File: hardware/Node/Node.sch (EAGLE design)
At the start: 67 parts, among them J1 AVR_SPI_PRG_6NS, J2 M04X2, Q1 PMR280UN, Q2 PMR280UN, Q3 PMR280UN, SW1 KSS, SW2 KSS, U1 ATMEGA32U4QFN, U2 BLUETOOTH-RN41", U3 LSM303DLM, U4 L3GD20, U5 8.0MHz, U6 MCP73871, U7 V_REG_LDOSMD, U9 RCLAMP0502A, X1 USBSMD

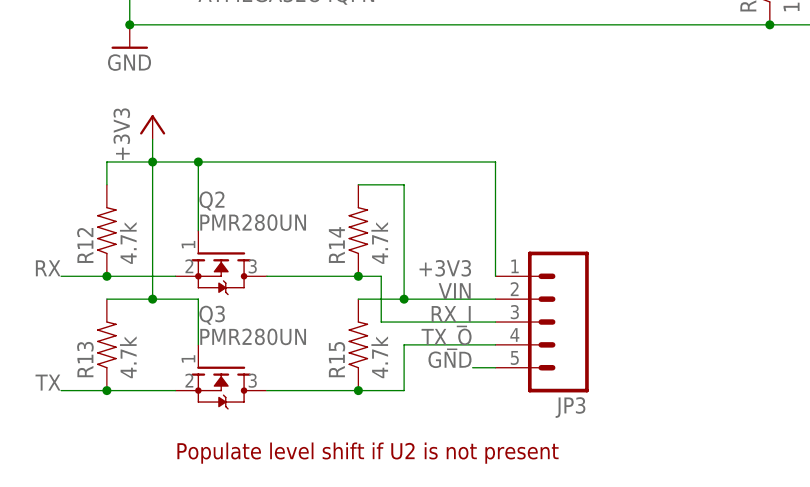
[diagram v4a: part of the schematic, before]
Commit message: put vbus on the header
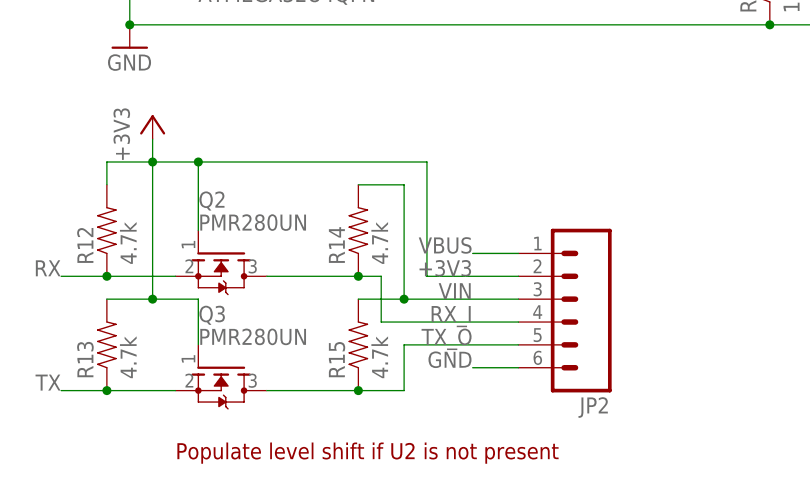
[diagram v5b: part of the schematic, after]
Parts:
- removed JP3: (no value), SparkFun:M05PTH
- added JP2: (no value), SparkFun:M06SIP
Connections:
- net +3V3: now also JP2.2; no longer JP3.1
- net GND: now also JP2.6; no longer JP3.5
- net RX_I: now also JP2.4; no longer JP3.3
- net TX_O: now also JP2.5; no longer JP3.4
- net VBUS: now also JP2.1
- net VIN: now also JP2.3; no longer JP3.2
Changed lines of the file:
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@@
 <grid distance="0.1" unitdist="inch" unit="inch" style="lines" multiple="1" display="no" altdistance="0.01" altunitdist="inch" altunit="inch"/>
 <layers>
-<layer number="1" name="Top" color="4" fill="1" visible="yes" active="no"/>
-<layer number="16" name="Bottom" color="1" fill="1" visible="yes" active="no"/>
-<layer number="17" name="Pads" color="2" fill="1" visible="yes" active="no"/>
-<layer number="18" name="Vias" color="2" fill="1" visible="yes" active="no"/>
-<layer number="19" name="Unrouted" color="6" fill="1" visible="yes" active="no"/>
-<layer number="20" name="Dimension" color="15" fill="1" visible="yes" active="no"/>
-<layer number="21" name="tPlace" color="7" fill="1" visible="yes" active="no"/>
-<layer number="22" name="bPlace" color="7" fill="1" visible="yes" active="no"/>
-<layer number="23" name="tOrigins" color="15" fill="1" visible="yes" active="no"/>
-<layer number="24" name="bOrigins" color="15" fill="1" visible="yes" active="no"/>
-<layer number="25" name="tNames" color="7" fill="1" visible="yes" active="no"/>
-<layer number="26" name="bNames" color="7" fill="1" visible="yes" active="no"/>
-<layer number="27" name="tValues" color="7" fill="1" visible="yes" active="no"/>
-<layer number="28" name="bValues" color="7" fill="1" visible="yes" active="no"/>
+<layer number="1" name="Top" color="4" fill="1" visible="no" active="no"/>
+<layer number="16" name="Bottom" color="1" fill="1" visible="no" active="no"/>
+<layer number="17" name="Pads" color="2" fill="1" visible="no" active="no"/>
+<layer number="18" name="Vias" color="2" fill="1" visible="no" active="no"/>
+<layer number="19" name="Unrouted" color="6" fill="1" visible="no" active="no"/>
+<layer number="20" name="Dimension" color="15" fill="1" visible="no" active="no"/>
+<layer number="21" name="tPlace" color="7" fill="1" visible="no" active="no"/>
+<layer number="22" name="bPlace" color="7" fill="1" visible="no" active="no"/>
+<layer number="23" name="tOrigins" color="15" fill="1" visible="no" active="no"/>
+<layer number="24" name="bOrigins" color="15" fill="1" visible="no" active="no"/>
+<layer number="25" name="tNames" color="7" fill="1" visible="no" active="no"/>
+<layer number="26" name="bNames" color="7" fill="1" visible="no" active="no"/>
+<layer number="27" name="tValues" color="7" fill="1" visible="no" active="no"/>
+<layer number="28" name="bValues" color="7" fill="1" visible="no" active="no"/>
 <layer number="29" name="tStop" color="7" fill="3" visible="no" active="no"/>
 <layer number="30" name="bStop" color="7" fill="6" visible="no" active="no"/>
@@
 <layer number="35" name="tGlue" color="7" fill="4" visible="no" active="no"/>
 <layer number="36" name="bGlue" color="7" fill="5" visible="no" active="no"/>
-<layer number="37" name="tTest" color="7" fill="1" visible="yes" active="no"/>
-<layer number="38" name="bTest" color="7" fill="1" visible="yes" active="no"/>
+<layer number="37" name="tTest" color="7" fill="1" visible="no" active="no"/>
+<layer number="38" name="bTest" color="7" fill="1" visible="no" active="no"/>
 <layer number="39" name="tKeepout" color="4" fill="11" visible="no" active="no"/>
 <layer number="40" name="bKeepout" color="1" fill="11" visible="no" active="no"/>
@@
 <layer number="44" name="Drills" color="7" fill="1" visible="no" active="no"/>
 <layer number="45" name="Holes" color="7" fill="1" visible="no" active="no"/>
-<layer number="46" name="Milling" color="3" fill="1" visible="yes" active="no"/>
-<layer number="47" name="Measures" color="7" fill="1" visible="yes" active="no"/>
-<layer number="48" name="Document" color="7" fill="1" visible="yes" active="no"/>
-<layer number="49" name="Reference" color="7" fill="1" visible="yes" active="no"/>
-<layer number="50" name="dxf" color="7" fill="1" visible="yes" active="no"/>
-<layer number="51" name="tDocu" color="7" fill="1" visible="yes" active="no"/>
-<layer number="52" name="bDocu" color="7" fill="1" visible="yes" active="no"/>
-<layer number="53" name="tGND_GNDA" color="7" fill="9" visible="yes" active="no"/>
-<layer number="54" name="bGND_GNDA" color="1" fill="9" visible="yes" active="no"/>
-<layer number="56" name="wert" color="7" fill="1" visible="yes" active="no"/>
+<layer number="46" name="Milling" color="3" fill="1" visible="no" active="no"/>
+<layer number="47" name="Measures" color="7" fill="1" visible="no" active="no"/>
+<layer number="48" name="Document" color="7" fill="1" visible="no" active="no"/>
+<layer number="49" name="Reference" color="7" fill="1" visible="no" active="no"/>
+<layer number="50" name="dxf" color="7" fill="1" visible="no" active="no"/>
+<layer number="51" name="tDocu" color="7" fill="1" visible="no" active="no"/>
+<layer number="52" name="bDocu" color="7" fill="1" visible="no" active="no"/>
+<layer number="53" name="tGND_GNDA" color="7" fill="9" visible="no" active="no"/>
+<layer number="54" name="bGND_GNDA" color="1" fill="9" visible="no" active="no"/>
+<layer number="56" name="wert" color="7" fill="1" visible="no" active="no"/>
 <layer number="91" name="Nets" color="2" fill="1" visible="yes" active="yes"/>
 <layer number="92" name="Busses" color="1" fill="1" visible="yes" active="yes"/>
@@
 <part name="LED1" library="SparkFun" deviceset="LED" device="0603"/>
 <part name="R20" library="SparkFun" deviceset="RESISTOR" device="0402-RES" value="1k"/>
-<part name="JP3" library="SparkFun" deviceset="M05" device="PTH"/>
 <part name="R10" library="SparkFun" deviceset="RESISTOR" device="0402-RES" value="100k"/>
 <part name="R11" library="SparkFun" deviceset="RESISTOR" device="0402-RES" value="100k"/>
 <part name="J2" library="SparkFun" deviceset="M04X2" device=""/>
 <part name="+3V9" library="supply1" deviceset="+3V3" device=""/>
+<part name="JP2" library="SparkFun" deviceset="M06" device="SIP"/>
 </parts>
 <sheets>
@@
 <instance part="LED1" gate="G$1" x="50.8" y="203.2"/>
 <instance part="R20" gate="G$1" x="50.8" y="193.04" rot="R90"/>
-<instance part="JP3" gate="G$1" x="147.32" y="20.32" rot="R180"/>
 <instance part="R10" gate="G$1" x="157.48" y="187.96" rot="R90"/>
 <instance part="R11" gate="G$1" x="157.48" y="172.72" rot="R90"/>
 <instance part="J2" gate="G$1" x="160.02" y="132.08"/>
 <instance part="+3V9" gate="G$1" x="149.86" y="139.7"/>
+<instance part="JP2" gate="G$1" x="147.32" y="22.86" rot="R180"/>
 </instances>
 <busses>
@@
 </segment>
 <segment>
-<wire x1="139.7" y1="15.24" x2="137.16" y2="15.24" width="0.1524" layer="91"/>
+<wire x1="142.24" y1="15.24" x2="137.16" y2="15.24" width="0.1524" layer="91"/>
 <label x="137.16" y="15.24" size="1.778" layer="95" rot="MR0"/>
-<pinref part="JP3" gate="G$1" pin="5"/>
+<pinref part="JP2" gate="G$1" pin="6"/>
 </segment>
 <segment>
@@
 <wire x1="96.52" y1="35.56" x2="96.52" y2="38.1" width="0.1524" layer="91"/>
 <wire x1="96.52" y1="38.1" x2="101.6" y2="38.1" width="0.1524" layer="91"/>
-<wire x1="106.68" y1="38.1" x2="139.7" y2="38.1" width="0.1524" layer="91"/>
+<wire x1="106.68" y1="38.1" x2="132.08" y2="38.1" width="0.1524" layer="91"/>
+<wire x1="132.08" y1="38.1" x2="132.08" y2="25.4" width="0.1524" layer="91"/>
 <junction x="106.68" y="38.1"/>
-<pinref part="JP3" gate="G$1" pin="1"/>
-<wire x1="139.7" y1="38.1" x2="139.7" y2="25.4" width="0.1524" layer="91"/>
+<pinref part="JP2" gate="G$1" pin="2"/>
+<wire x1="132.08" y1="25.4" x2="142.24" y2="25.4" width="0.1524" layer="91"/>
 <label x="137.16" y="25.4" size="1.778" layer="95" rot="MR0"/>
 </segment>
@@
 <pinref part="U9" gate="G$1" pin="VCC"/>
 </segment>
+<segment>
+<pinref part="JP2" gate="G$1" pin="1"/>
+<wire x1="142.24" y1="27.94" x2="137.16" y2="27.94" width="0.1524" layer="91"/>
+<label x="137.16" y="27.94" size="1.778" layer="95" rot="MR0"/>
+</segment>
 </net>
 <net name="RX" class="0">
@@
 <pinref part="R14" gate="G$1" pin="1"/>
 <wire x1="124.46" y1="25.4" x2="114.3" y2="25.4" width="0.1524" layer="91"/>
-<wire x1="139.7" y1="20.32" x2="127" y2="20.32" width="0.1524" layer="91"/>
+<wire x1="142.24" y1="20.32" x2="127" y2="20.32" width="0.1524" layer="91"/>
 <wire x1="127" y1="20.32" x2="127" y2="25.4" width="0.1524" layer="91"/>
 <wire x1="127" y1="25.4" x2="124.46" y2="25.4" width="0.1524" layer="91"/>
 <junction x="124.46" y="25.4"/>
 <label x="137.16" y="20.32" size="1.778" layer="95" rot="MR0"/>
-<pinref part="JP3" gate="G$1" pin="3"/>
+<pinref part="JP2" gate="G$1" pin="4"/>
 </segment>
 </net>
@@
 <pinref part="R15" gate="G$1" pin="1"/>
 <wire x1="124.46" y1="12.7" x2="114.3" y2="12.7" width="0.1524" layer="91"/>
-<wire x1="139.7" y1="17.78" x2="129.54" y2="17.78" width="0.1524" layer="91"/>
+<wire x1="142.24" y1="17.78" x2="129.54" y2="17.78" width="0.1524" layer="91"/>
 <wire x1="129.54" y1="17.78" x2="129.54" y2="12.7" width="0.1524" layer="91"/>
 <wire x1="129.54" y1="12.7" x2="124.46" y2="12.7" width="0.1524" layer="91"/>
 <junction x="124.46" y="12.7"/>
 <label x="137.16" y="17.78" size="1.778" layer="95" rot="MR0"/>
-<pinref part="JP3" gate="G$1" pin="4"/>
+<pinref part="JP2" gate="G$1" pin="5"/>
 </segment>
 </net>
@@
 <segment>
 <pinref part="R15" gate="G$1" pin="2"/>
-<wire x1="139.7" y1="22.86" x2="129.54" y2="22.86" width="0.1524" layer="91"/>
+<wire x1="142.24" y1="22.86" x2="129.54" y2="22.86" width="0.1524" layer="91"/>
 <pinref part="R14" gate="G$1" pin="2"/>
 <wire x1="129.54" y1="22.86" x2="124.46" y2="22.86" width="0.1524" layer="91"/>
@@
 <junction x="129.54" y="22.86"/>
 <label x="137.16" y="22.86" size="1.778" layer="95" rot="MR0"/>
-<pinref part="JP3" gate="G$1" pin="2"/>
-</segment>
-</net>
+<pinref part="JP2" gate="G$1" pin="3"/>
+</segment>
+</net>

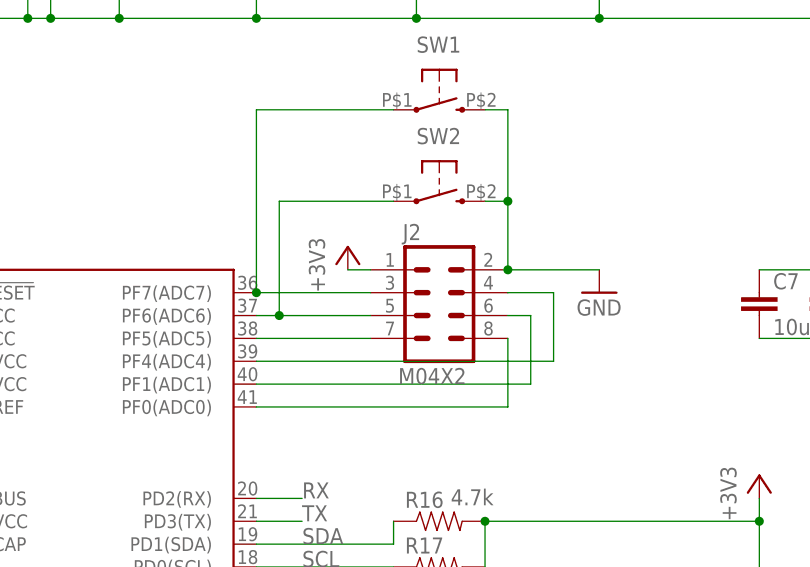
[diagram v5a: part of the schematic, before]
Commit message: route more of the breakouts
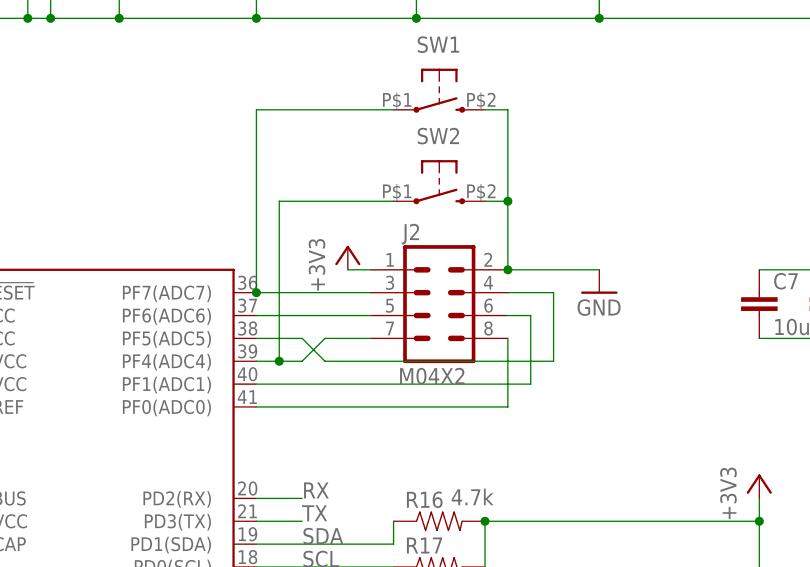
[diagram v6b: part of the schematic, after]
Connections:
- removed net N$31: J2.5, SW2.1, U1.PF6(ADC6)
- removed net N$33: J2.4, U1.PF4(ADC4)
- new net N$15: J2.4, U1.PF5(ADC5)
- new net N$30: J2.7, SW2.1, U1.PF4(ADC4)
- net N$32: now also J2.5, U1.PF6(ADC6); no longer J2.7, U1.PF5(ADC5)
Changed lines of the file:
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@@
-</segment>
-</net>
-<net name="N$31" class="0">
-<segment>
-<pinref part="U1" gate="G$1" pin="PF6(ADC6)"/>
-<wire x1="139.7" y1="132.08" x2="142.24" y2="132.08" width="0.1524" layer="91"/>
-<pinref part="SW2" gate="G$1" pin="1"/>
-<wire x1="142.24" y1="132.08" x2="152.4" y2="132.08" width="0.1524" layer="91"/>
-<wire x1="154.94" y1="144.78" x2="142.24" y2="144.78" width="0.1524" layer="91"/>
-<wire x1="142.24" y1="144.78" x2="142.24" y2="132.08" width="0.1524" layer="91"/>
-<junction x="142.24" y="132.08"/>
-<pinref part="J2" gate="G$1" pin="5"/>
-</segment>
-</net>
-<net name="N$32" class="0">
-<segment>
-<pinref part="U1" gate="G$1" pin="PF5(ADC5)"/>
-<wire x1="139.7" y1="129.54" x2="152.4" y2="129.54" width="0.1524" layer="91"/>
-<pinref part="J2" gate="G$1" pin="7"/>
-</segment>
-</net>
-<net name="N$33" class="0">
-<segment>
-<pinref part="U1" gate="G$1" pin="PF4(ADC4)"/>
-<wire x1="139.7" y1="127" x2="172.72" y2="127" width="0.1524" layer="91"/>
-<wire x1="172.72" y1="127" x2="172.72" y2="134.62" width="0.1524" layer="91"/>
-<wire x1="172.72" y1="134.62" x2="167.64" y2="134.62" width="0.1524" layer="91"/>
-<pinref part="J2" gate="G$1" pin="4"/>
 </segment>
 </net>
@@
 </segment>
 </net>
+<net name="N$15" class="0">
+<segment>
+<pinref part="U1" gate="G$1" pin="PF5(ADC5)"/>
+<wire x1="139.7" y1="129.54" x2="144.78" y2="129.54" width="0.1524" layer="91"/>
+<wire x1="172.72" y1="127" x2="172.72" y2="134.62" width="0.1524" layer="91"/>
+<wire x1="172.72" y1="134.62" x2="167.64" y2="134.62" width="0.1524" layer="91"/>
+<pinref part="J2" gate="G$1" pin="4"/>
+<wire x1="144.78" y1="129.54" x2="147.32" y2="127" width="0.1524" layer="91"/>
+<wire x1="147.32" y1="127" x2="172.72" y2="127" width="0.1524" layer="91"/>
+</segment>
+</net>
+<net name="N$32" class="0">
+<segment>
+<pinref part="J2" gate="G$1" pin="5"/>
+<pinref part="U1" gate="G$1" pin="PF6(ADC6)"/>
+<wire x1="139.7" y1="132.08" x2="152.4" y2="132.08" width="0.1524" layer="91"/>
+</segment>
+</net>
+<net name="N$30" class="0">
+<segment>
+<pinref part="SW2" gate="G$1" pin="1"/>
+<wire x1="154.94" y1="144.78" x2="142.24" y2="144.78" width="0.1524" layer="91"/>
+<pinref part="U1" gate="G$1" pin="PF4(ADC4)"/>
+<wire x1="139.7" y1="127" x2="142.24" y2="127" width="0.1524" layer="91"/>
+<pinref part="J2" gate="G$1" pin="7"/>
+<wire x1="142.24" y1="127" x2="144.78" y2="127" width="0.1524" layer="91"/>
+<wire x1="144.78" y1="127" x2="147.32" y2="129.54" width="0.1524" layer="91"/>
+<wire x1="147.32" y1="129.54" x2="152.4" y2="129.54" width="0.1524" layer="91"/>
+<wire x1="142.24" y1="144.78" x2="142.24" y2="127" width="0.1524" layer="91"/>
+<junction x="142.24" y="127"/>
+</segment>
+</net>
